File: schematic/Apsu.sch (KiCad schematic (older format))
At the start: 36 parts

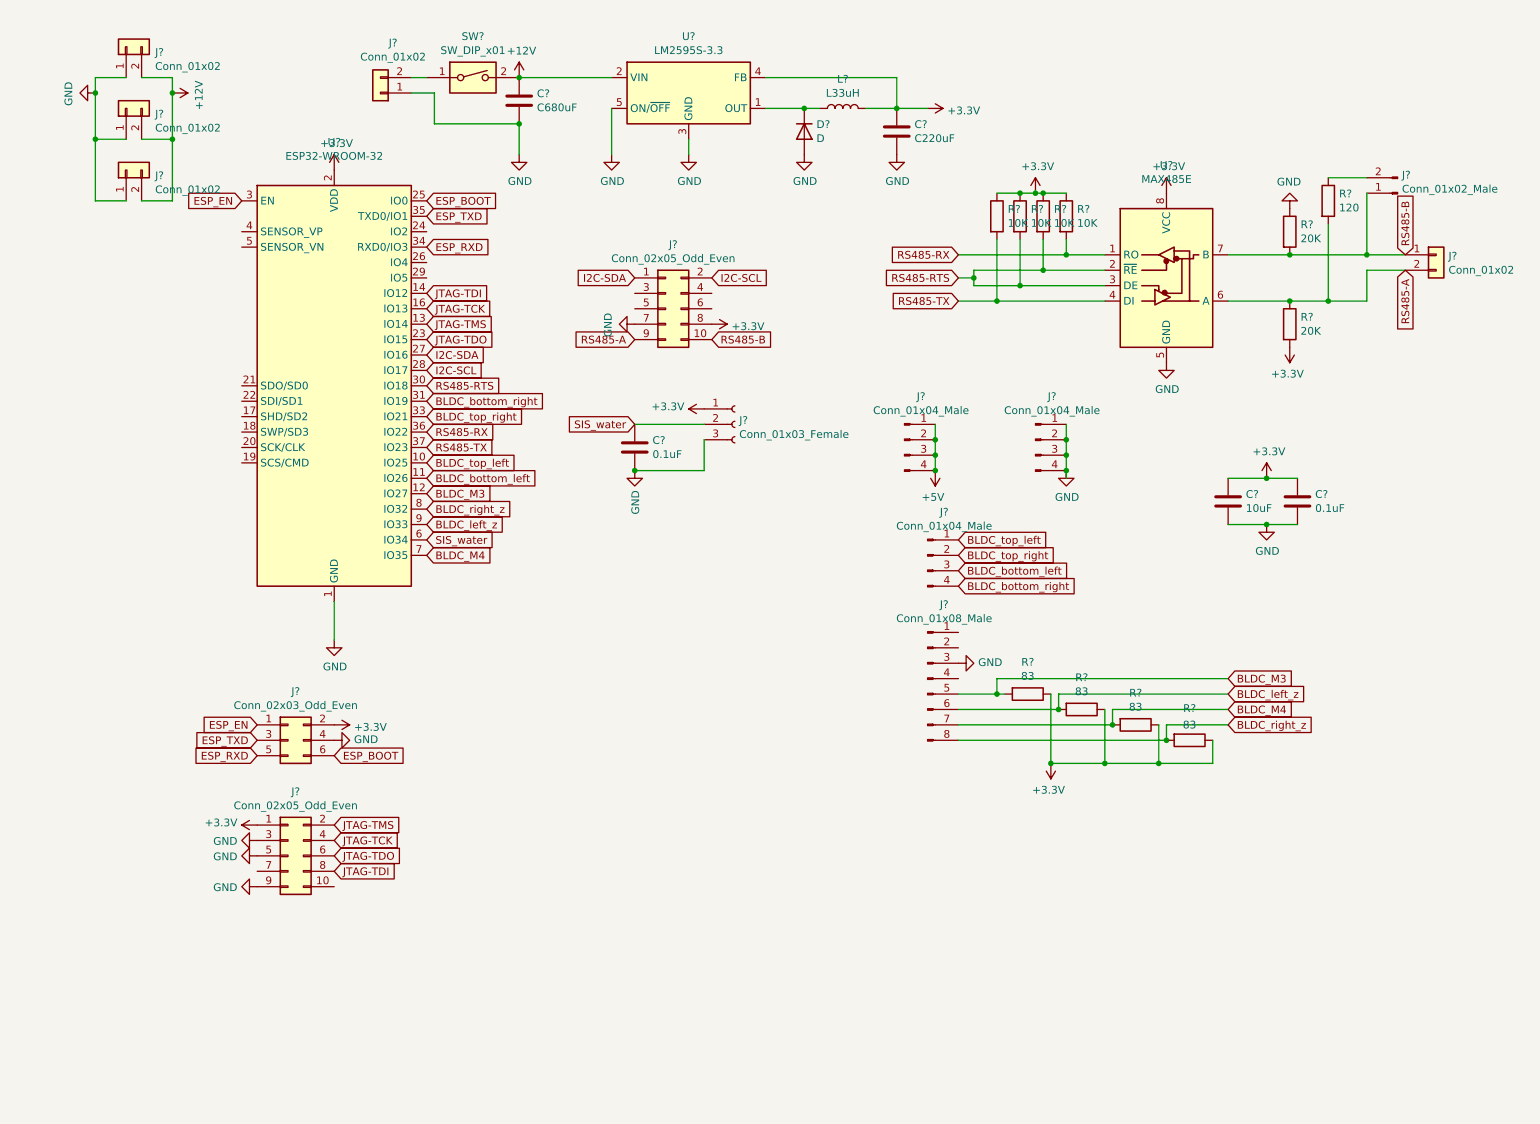
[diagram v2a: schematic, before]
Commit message: SIS water to I2C and added SPI
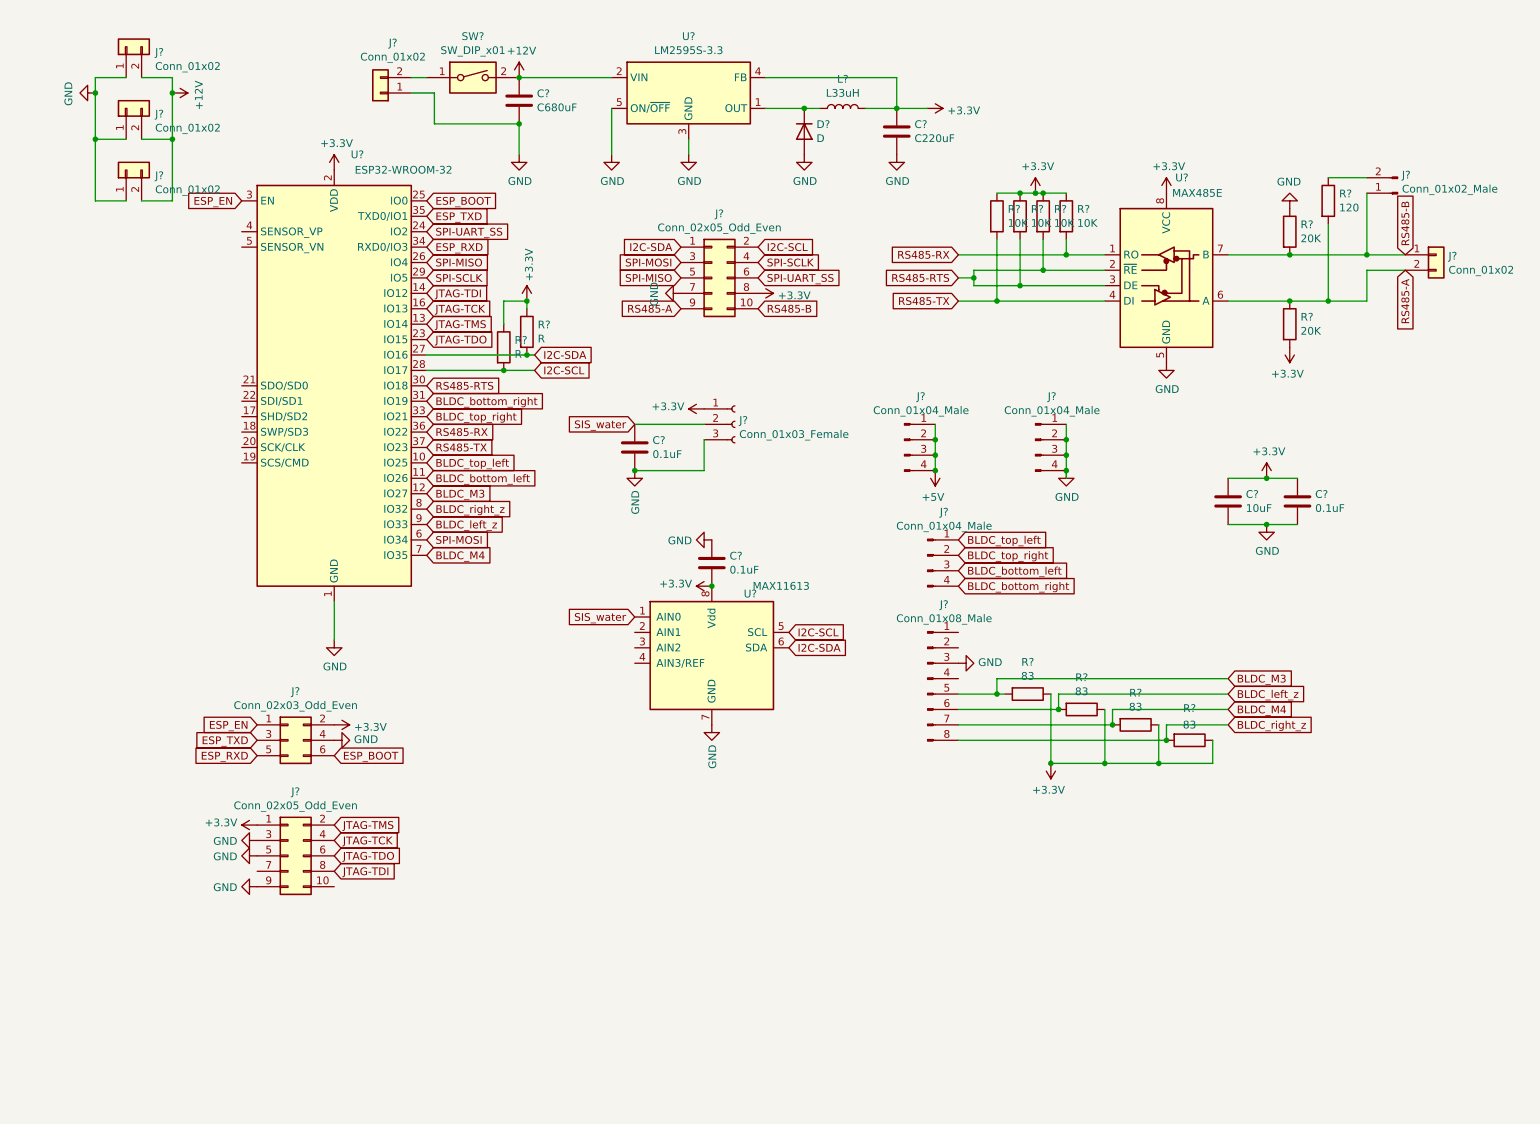
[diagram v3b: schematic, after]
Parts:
- added C?: 0.1uF, symbol Device:C
- added R? (x2): R, symbol Device:R
- added U?: MAX11613, Package_SO:MSOP-8_3x3mm_P0.65mm, symbol Analog_ADC:MAX11613
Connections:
- net +3V3: now also C?.2, R?.1, R?.1, U?.8 (Vdd)
- net GND: now also C?.1, U?.7 (GND)
- net I2C-SCL: now also R?.2, U?.5 (SCL)
- net I2C-SDA: now also R?.2, U?.6 (SDA)
- net SIS_water: now also U?.1 (AIN0); no longer U?.6 (IO34)
- net SPI-UART_SS: now reaches U?.24 (IO2)
- net SPI-UART_SS: now also J?.6 (Pin_6)
- net SPI-MISO: now reaches U?.26 (IO4)
- net SPI-MISO: now also J?.5 (Pin_5)
- net SPI-SCLK: now reaches U?.29 (IO5)
- net SPI-SCLK: now also J?.4 (Pin_4)
- net SPI-MOSI: now reaches J?.3 (Pin_3)
- net SPI-MOSI: now also U?.6 (IO34)
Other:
- moved on the sheet: J?
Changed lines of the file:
@@
 	1    0    0    -1
 $EndComp
-Text GLabel 3000 3950 2    50   Input ~ 0
-SIS_water
 $Comp
 L Interface_UART:MAX485E U?
 U 1 1 5ECE9CD6
 P 7800 2200
-F 0 "U?" H 7800 2881 50  0000 C CNN
-F 1 "MAX485E" H 7800 2790 50  0000 C CNN
+F 0 "U?" H 7900 2800 50  0000 C CNN
+F 1 "MAX485E" H 8000 2700 50  0000 C CNN
 F 2 "" H 7800 1500 50  0001 C CNN
 F 3 "https://datasheets.maximintegrated.com/en/ds/MAX1487E-MAX491E.pdf" H 7800 2250 50  0001 C CNN
@@
 	1    0    0    -1
 $EndComp
-$Comp
-L power:+3.3V #PWR?
-U 1 1 5EC52158
-P 7800 1700
-F 0 "#PWR?" H 7800 1550 50  0001 C CNN
-F 1 "+3.3V" H 7815 1873 50  0000 C CNN
-F 2 "" H 7800 1700 50  0001 C CNN
-F 3 "" H 7800 1700 50  0001 C CNN
-	1    7800 1700
-	1    0    0    -1
-$EndComp
 Wire Wire Line
 	8200 2400 8600 2400
@@
 U 1 1 5EBF8AC7
 P 2400 2950
-F 0 "U?" H 2400 4531 50  0000 C CNN
-F 1 "ESP32-WROOM-32" H 2400 4440 50  0000 C CNN
+F 0 "U?" H 2550 4450 50  0000 C CNN
+F 1 "ESP32-WROOM-32" H 2850 4350 50  0000 C CNN
 F 2 "RF_Module:ESP32-WROOM-32" H 2400 1450 50  0001 C CNN
 F 3 "https://www.espressif.com/sites/default/files/documentation/esp32-wroom-32_datasheet_en.pdf" H 2100 3000 50  0001 C CNN
@@
 L Connector_Generic:Conn_02x05_Odd_Even J?
 U 1 1 5ED317E1
-P 4550 2450
-F 0 "J?" H 4600 2867 50  0000 C CNN
-F 1 "Conn_02x05_Odd_Even" H 4600 2776 50  0000 C CNN
-F 2 "" H 4550 2450 50  0001 C CNN
-F 3 "~" H 4550 2450 50  0001 C CNN
-	1    4550 2450
-	1    0    0    -1
-$EndComp
-Text GLabel 3000 2750 2    50   Input ~ 0
+P 4850 2250
+F 0 "J?" H 4900 2667 50  0000 C CNN
+F 1 "Conn_02x05_Odd_Even" H 4900 2576 50  0000 C CNN
+F 2 "" H 4850 2250 50  0001 C CNN
+F 3 "~" H 4850 2250 50  0001 C CNN
+	1    4850 2250
+	1    0    0    -1
+$EndComp
+Text GLabel 3700 2750 2    50   Input ~ 0
 I2C-SDA
-Text GLabel 3000 2850 2    50   Input ~ 0
+Text GLabel 3700 2850 2    50   Input ~ 0
 I2C-SCL
-Text GLabel 4350 2250 0    50   Input ~ 0
+Text GLabel 4650 2050 0    50   Input ~ 0
 I2C-SDA
-Text GLabel 4850 2250 2    50   Input ~ 0
+Text GLabel 5150 2050 2    50   Input ~ 0
 I2C-SCL
 $Comp
 L power:GND #PWR?
 U 1 1 5ED5B109
-P 4350 2550
-F 0 "#PWR?" H 4350 2300 50  0001 C CNN
-F 1 "GND" H 4355 2377 50  0000 C CNN
-F 2 "" H 4350 2550 50  0001 C CNN
-F 3 "" H 4350 2550 50  0001 C CNN
-	1    4350 2550
+P 4650 2350
+F 0 "#PWR?" H 4650 2100 50  0001 C CNN
+F 1 "GND" H 4655 2177 50  0000 C CNN
+F 2 "" H 4650 2350 50  0001 C CNN
+F 3 "" H 4650 2350 50  0001 C CNN
+	1    4650 2350
 	0    1    1    0
 $EndComp
@@
 L power:+3.3V #PWR?
 U 1 1 5ED5B8B2
-P 4850 2550
-F 0 "#PWR?" H 4850 2400 50  0001 C CNN
-F 1 "+3.3V" V 4865 2678 50  0000 L CNN
-F 2 "" H 4850 2550 50  0001 C CNN
-F 3 "" H 4850 2550 50  0001 C CNN
-	1    4850 2550
+P 5150 2350
+F 0 "#PWR?" H 5150 2200 50  0001 C CNN
+F 1 "+3.3V" V 5165 2478 50  0000 L CNN
+F 2 "" H 5150 2350 50  0001 C CNN
+F 3 "" H 5150 2350 50  0001 C CNN
+	1    5150 2350
 	0    1    1    0
 $EndComp
@@
 Wire Wire Line
 	9100 2200 9350 2200
-Text GLabel 4350 2650 0    50   Input ~ 0
+Text GLabel 4650 2450 0    50   Input ~ 0
 RS485-A
-Text GLabel 4850 2650 2    50   Input ~ 0
+Text GLabel 5150 2450 2    50   Input ~ 0
 RS485-B
 $Comp
@@
 	6300 3300 6300 3200
 Connection ~ 6300 3300
+$Comp
+L Analog_ADC:MAX11613 U?
+U 1 1 5EC93959
+P 4850 4650
+F 0 "U?" H 5100 5000 50  0000 C CNN
+F 1 "MAX11613" H 5300 5050 50  0000 C CNN
+F 2 "Package_SO:MSOP-8_3x3mm_P0.65mm" H 5300 4300 50  0001 L CNN
+F 3 "https://datasheets.maximintegrated.com/en/ds/MAX11612-MAX11617.pdf" H 4950 5150 50  0001 C CNN
+	1    4850 4650
+	1    0    0    -1
+$EndComp
+Text GLabel 4350 4450 0    50   Input ~ 0
+SIS_water
+Text GLabel 5350 4650 2    50   Input ~ 0
+I2C-SDA
+Text GLabel 5350 4550 2    50   Input ~ 0
+I2C-SCL
+$Comp
+L power:GND #PWR?
+U 1 1 5EC95FBB
+P 4850 5150
+F 0 "#PWR?" H 4850 4900 50  0001 C CNN
+F 1 "GND" V 4855 5022 50  0000 R CNN
+F 2 "" H 4850 5150 50  0001 C CNN
+F 3 "" H 4850 5150 50  0001 C CNN
+	1    4850 5150
+	1    0    0    -1
+$EndComp
+$Comp
+L power:+3.3V #PWR?
+U 1 1 5EC9658D
+P 4850 4250
+F 0 "#PWR?" H 4850 4100 50  0001 C CNN
+F 1 "+3.3V" V 4865 4378 50  0000 L CNN
+F 2 "" H 4850 4250 50  0001 C CNN
+F 3 "" H 4850 4250 50  0001 C CNN
+	1    4850 4250
+	0    -1   -1   0
+$EndComp
+$Comp
+L power:+3.3V #PWR?
+U 1 1 5ECA2233
+P 3650 2400
+F 0 "#PWR?" H 3650 2250 50  0001 C CNN
+F 1 "+3.3V" V 3665 2528 50  0000 L CNN
+F 2 "" H 3650 2400 50  0001 C CNN
+F 3 "" H 3650 2400 50  0001 C CNN
+	1    3650 2400
+	1    0    0    -1
+$EndComp
+Wire Wire Line
+	3700 2750 3650 2750
+$Comp
+L Device:R R?
+U 1 1 5ECC0470
+P 3500 2700
+F 0 "R?" H 3570 2746 50  0000 L CNN
+F 1 "R" H 3570 2655 50  0000 L CNN
+F 2 "" V 3430 2700 50  0001 C CNN
+F 3 "~" H 3500 2700 50  0001 C CNN
+	1    3500 2700
+	1    0    0    -1
+$EndComp
+Connection ~ 3500 2850
+Wire Wire Line
+	3500 2850 3000 2850
+$Comp
+L Device:R R?
+U 1 1 5ECC587C
+P 3650 2600
+F 0 "R?" H 3720 2646 50  0000 L CNN
+F 1 "R" H 3720 2555 50  0000 L CNN
+F 2 "" V 3580 2600 50  0001 C CNN
+F 3 "~" H 3650 2600 50  0001 C CNN
+	1    3650 2600
+	1    0    0    -1
+$EndComp
+Connection ~ 3650 2750
+Wire Wire Line
+	3650 2750 3000 2750
+Wire Wire Line
+	3500 2550 3500 2400
+Wire Wire Line
+	3500 2400 3650 2400
+Wire Wire Line
+	3650 2450 3650 2400
+Connection ~ 3650 2400
+Wire Wire Line
+	3500 2850 3700 2850
+$Comp
+L Device:C C?
+U 1 1 5ECDE2A9
+P 4850 4100
+F 0 "C?" H 4965 4146 50  0000 L CNN
+F 1 "0.1uF" H 4965 4055 50  0000 L CNN
+F 2 "" H 4888 3950 50  0001 C CNN
+F 3 "~" H 4850 4100 50  0001 C CNN
+	1    4850 4100
+	1    0    0    -1
+$EndComp
+Connection ~ 4850 4250
+$Comp
+L power:GND #PWR?
+U 1 1 5ECDF4E3
+P 4850 3950
+F 0 "#PWR?" H 4850 3700 50  0001 C CNN
+F 1 "GND" V 4855 3822 50  0000 R CNN
+F 2 "" H 4850 3950 50  0001 C CNN
+F 3 "" H 4850 3950 50  0001 C CNN
+	1    4850 3950
+	0    1    1    0
+$EndComp
+$Comp
+L power:+3.3V #PWR?
+U 1 1 5EC52158
+P 7800 1700
+F 0 "#PWR?" H 7800 1550 50  0001 C CNN
+F 1 "+3.3V" H 7815 1873 50  0000 C CNN
+F 2 "" H 7800 1700 50  0001 C CNN
+F 3 "" H 7800 1700 50  0001 C CNN
+	1    7800 1700
+	1    0    0    -1
+$EndComp
+Text GLabel 3000 3950 2    50   Input ~ 0
+SPI-MOSI
+Text GLabel 3000 2150 2    50   Input ~ 0
+SPI-MISO
+Text GLabel 3000 2250 2    50   Input ~ 0
+SPI-SCLK
+Text GLabel 3000 1950 2    50   Input ~ 0
+SPI-UART_SS
+Text GLabel 4650 2150 0    50   Input ~ 0
+SPI-MOSI
+Text GLabel 4650 2250 0    50   Input ~ 0
+SPI-MISO
+Text GLabel 5150 2150 2    50   Input ~ 0
+SPI-SCLK
+Text GLabel 5150 2250 2    50   Input ~ 0
+SPI-UART_SS
 $EndSCHEMATC
